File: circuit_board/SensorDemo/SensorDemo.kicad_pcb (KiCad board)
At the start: 2 copper layers, 65 x 57.5 mm, 43 parts, among them K1 PB, P1 CONN3X2, P2 CONN3X2, U1 TLV1117-33CDCYR, U2 dsPIC33EP32GP502, U3 LTC1658, U4 INA126, U5 REF1925, U6 REF1925, X1 CRYSTAL

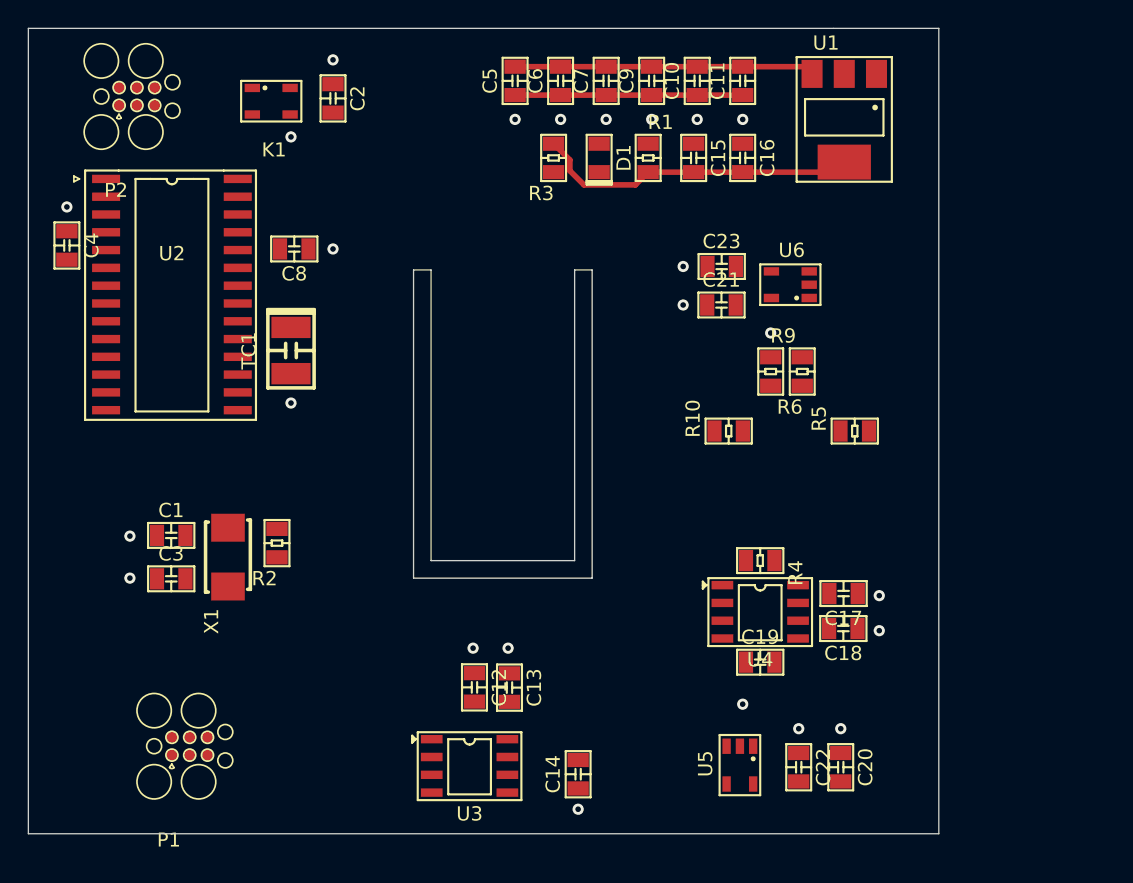
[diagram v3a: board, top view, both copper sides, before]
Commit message: symbol and pcb footprint updated
Added test points to replace the sensors.
TC2030 part modified.
the button needs modification.
TG connector:
https://www.tag-connect.com/product/tc2030-alt-nl-no-legs-cable-for-use-with-altera-usb-blaster
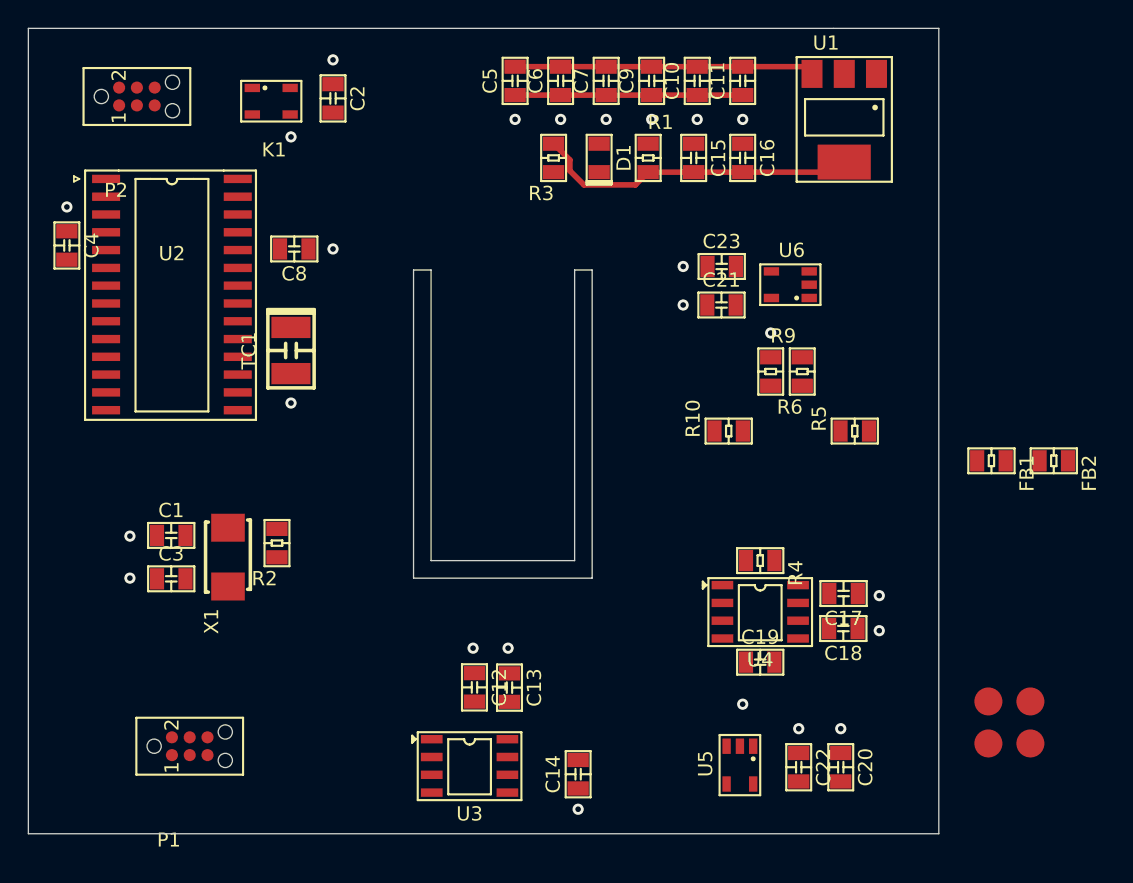
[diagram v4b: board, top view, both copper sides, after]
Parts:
- added FB1: 12.3071 nano ohm, SensorDemo_pcb:R0805, F.Cu at (186.3, 98.4)
- added FB2: 12.3071 nano ohm, SensorDemo_pcb:R0805, F.Cu at (190.7, 98.4)
- added TP1: TP, SensorDemo_pcb:TP_SMD_2MM, F.Cu at (186.0, 115.6)
- added TP2: TP, SensorDemo_pcb:TP_SMD_2MM, F.Cu at (186.0, 118.6)
- added TP3: TP, SensorDemo_pcb:TP_SMD_2MM, F.Cu at (189.0, 115.6)
- added TP4: TP, SensorDemo_pcb:TP_SMD_2MM, F.Cu at (189.0, 118.6)
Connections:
- K1 pad 1: Net-(K1-Pad1) -> (no net)
- K1 pad 3: Net-(K1-Pad3) -> (no net)
- P1 pad 1: (no net) -> /~MCLR
- P1 pad 2: (no net) -> /VDD
- P1 pad 4: (no net) -> /PGD
- P1 pad 5: (no net) -> /PGC
- P2 pad 1: (no net) -> /~MCLR
- P2 pad 2: (no net) -> /VDD
- P2 pad 3: (no net) -> GND
- P2 pad 4: (no net) -> /ucTX
- P2 pad 6: (no net) -> /ucRX
- U2 pad 10: Net-(U2-Pad10) -> (no net)
- U2 pad 11: Net-(U2-Pad11) -> (no net)
- U2 pad 12: Net-(U2-Pad12) -> (no net)
- U2 pad 14: Net-(U2-Pad14) -> (no net)
- U2 pad 18: Net-(U2-Pad18) -> (no net)
- U2 pad 23: Net-(U2-Pad23) -> (no net)
- U2 pad 24: Net-(U2-Pad24) -> (no net)
- U2 pad 25: Net-(U2-Pad25) -> (no net)
- U2 pad 26: Net-(U2-Pad26) -> (no net)
- U2 pad 3: Net-(U2-Pad3) -> (no net)
- U2 pad 9: Net-(U2-Pad9) -> (no net)
- U3 pad 4: Net-(U3-Pad4) -> (no net)
- U6 pad 1: Net-(U6-Pad1) -> (no net)
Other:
- copper layers 2 -> 4
- net class Default: clearance 0.2 -> 0.1524; trace_width 0.25 -> 0.1524; via_dia 0.8 -> 0.4; via_drill 0.4 -> 0.3
- rule trace_clearance: 0.2 -> 0.1524
- rule trace_min: 0.2 -> 0.1524
- rule via_min_size: 0.4 -> 0.3

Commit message: updated schematic
-fixed footprints
-spread parts
-connected some traces
- found FB (1kOhm, 1A)
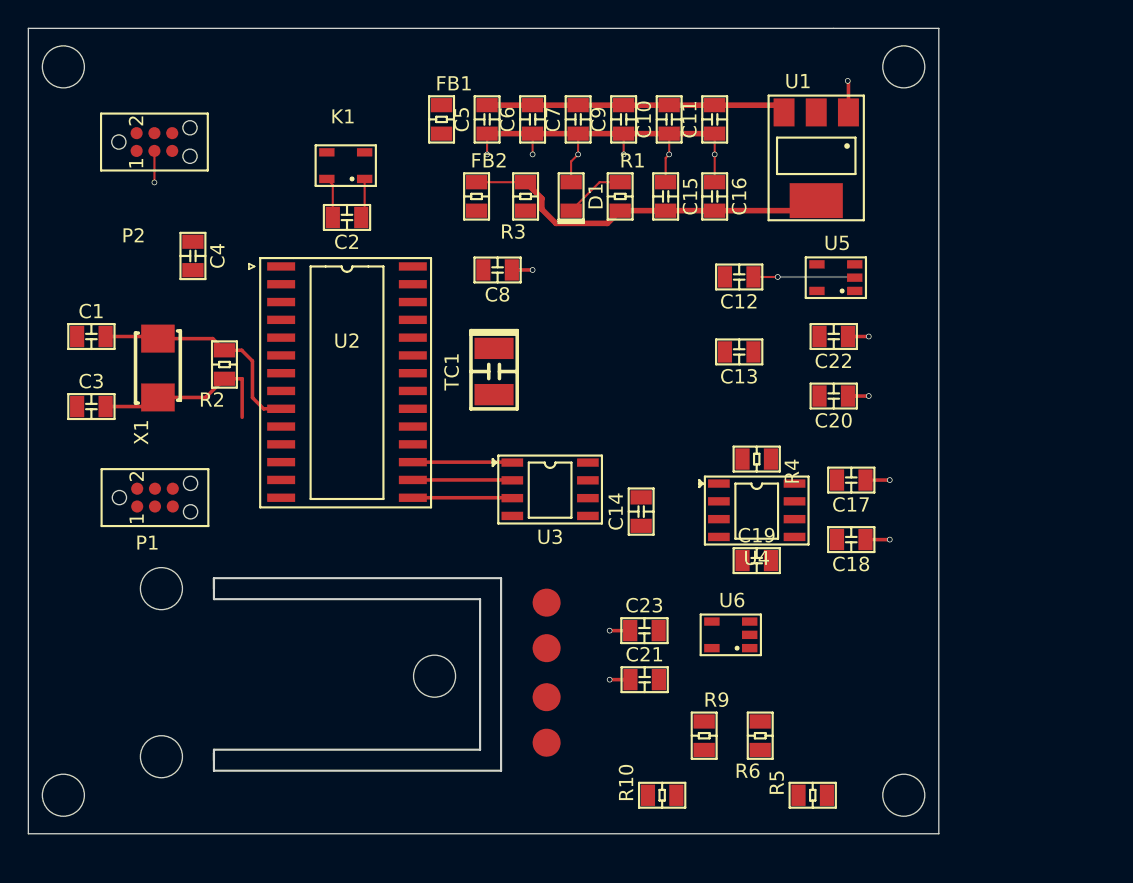
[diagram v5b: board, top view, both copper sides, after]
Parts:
- added MH1: MH, SensorDemo_pcb:MH_3MM, F.Cu at (120.0, 122.2)
- added MH2: MH, SensorDemo_pcb:MH_3MM, F.Cu at (127.0, 107.5)
- added MH3: MH, SensorDemo_pcb:MH_3MM, F.Cu at (180.0, 122.2)
- added MH4: MH, SensorDemo_pcb:MH_3MM, F.Cu at (127.0, 119.5)
- added MH5: MH, SensorDemo_pcb:MH_3MM, F.Cu at (120.0, 70.2)
- added MH6: MH, SensorDemo_pcb:MH_3MM, F.Cu at (146.5, 113.8)
- added MH7: MH, SensorDemo_pcb:MH_3MM, F.Cu at (180.0, 70.2)
- moved FB1 46.2 mm to (147.0, 74.0), turned to 90 degrees
- moved FB2 45.3 mm to (149.5, 79.5), turned to 90 degrees
- moved C12 34.9 mm to (168.2, 85.2), turned to 0 degrees
- moved TP3 34.7 mm to (154.5, 111.8)
- moved TP4 34.5 mm to (154.5, 118.5)
- moved U5 33.3 mm to (176.5, 86.2), turned to 180 degrees
- moved TP1 32.3 mm to (154.5, 108.5)
- moved TP2 31.7 mm to (154.5, 115.2)
- moved C22 30.9 mm to (175.0, 89.5), turned to 0 degrees
- moved C13 29.0 mm to (168.2, 90.6), turned to 0 degrees
- moved C21 27.3 mm to (161.5, 114.0)
- moved C23 26.6 mm to (161.5, 110.5)
- moved C20 26.5 mm to (175.0, 93.8), turned to 0 degrees
- moved R10 26.4 mm to (162.8, 122.2)
- moved R9 26.4 mm to (165.8, 118.0)
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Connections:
- C1 pad 1: Net-(C1-Pad1) -> /OSC1
- R2 pad 1: Net-(C1-Pad1) -> /OSC1
- U2 pad 10: (no net) -> /OSC1
- U2 pad 9: (no net) -> /OSC1
- X1 pad 1: Net-(C1-Pad1) -> /OSC1
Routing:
- net GND: track 16.2 -> 56.9 mm, vias 0 -> 16
- net /OSC1: track 0.00 -> 16.2 mm
- net Net-(C3-Pad1): track 0.00 -> 13.3 mm
- net Net-(U2-Pad17): track 0.00 -> 7.11 mm
- net Net-(U2-Pad16): track 0.00 -> 7.11 mm
- net Net-(U2-Pad15): track 0.00 -> 7.11 mm
- net Net-(D1-Pad1): track 0.00 -> 4.34 mm
- net +3V3: track 23.3 -> 26.8 mm
- net Net-(C2-Pad1): track 0.00 -> 2.93 mm
- net (no net): vias 24 -> 0
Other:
- outline, holes or cut-outs redrawn

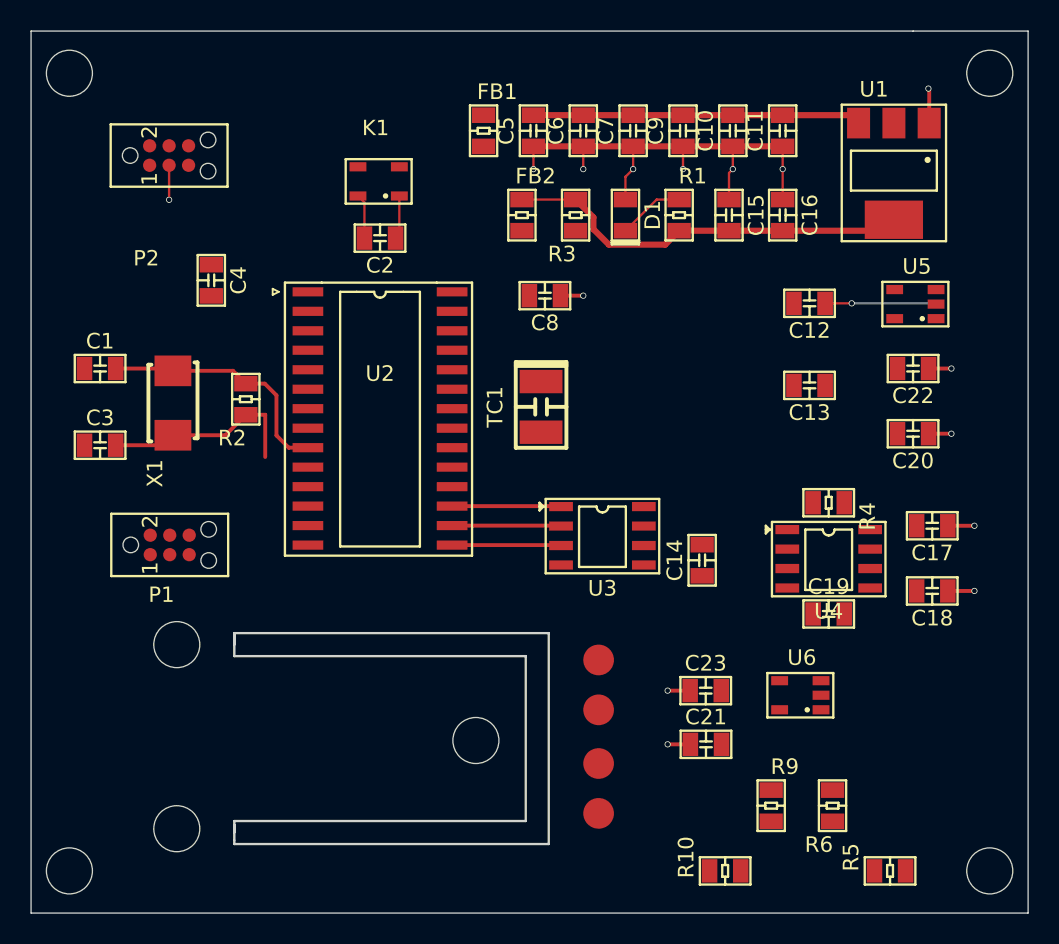
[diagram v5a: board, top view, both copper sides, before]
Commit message: update pcb
-connected traces
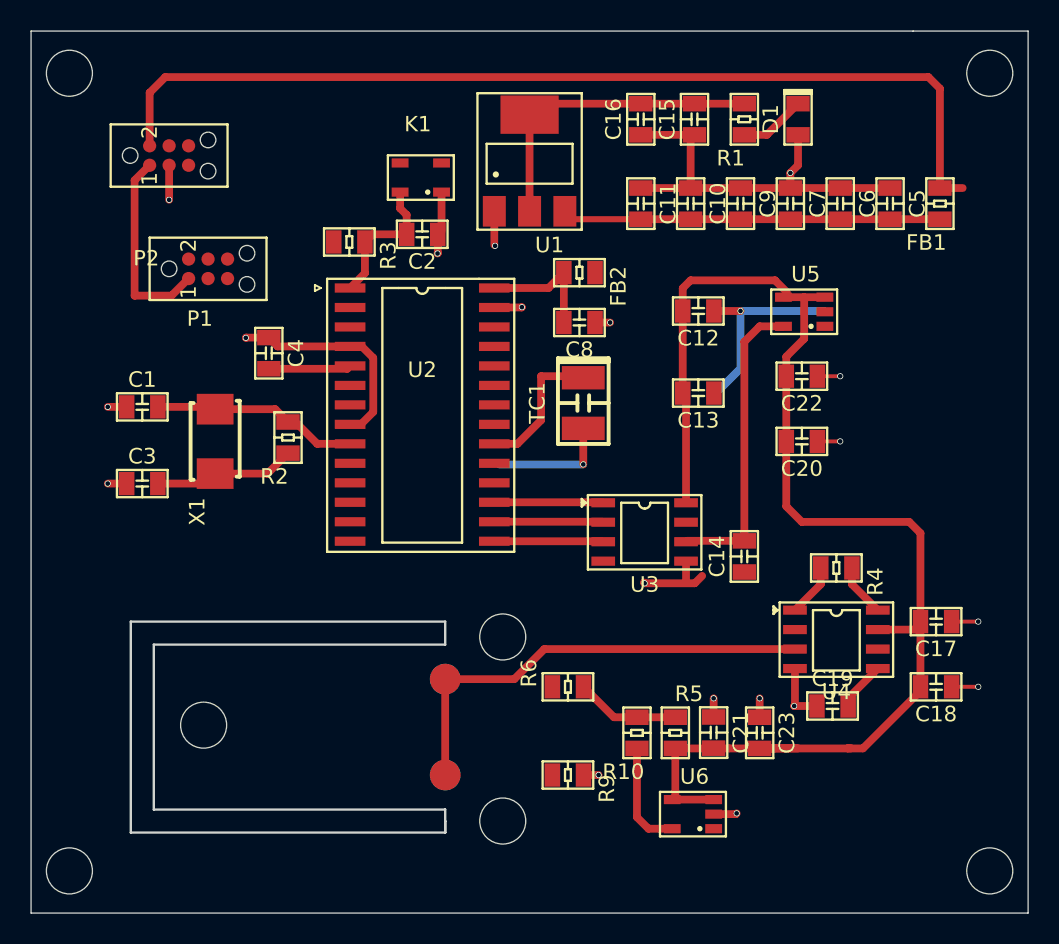
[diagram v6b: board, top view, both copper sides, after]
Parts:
- TP1, TP4: moved to B.Cu
- moved FB1 30.1 mm to (176.8, 78.8), turned to 270 degrees
- moved MH4 24.7 mm to (148.2, 107.0), turned to 180 degrees
- moved U1 24.4 mm to (150.0, 79.2), turned to 0 degrees
- moved MH2 24.2 mm to (148.2, 119.0), turned to 180 degrees
- moved C5 23.7 mm to (173.5, 78.8), turned to 90 degrees
- moved R6 18.9 mm to (152.5, 110.2), turned to 180 degrees
- moved P1 18.2 mm to (126.5, 83.0)
- moved MH6 17.8 mm to (128.8, 112.8), turned to 180 degrees
- moved C6 17.4 mm to (170.2, 78.8), turned to 90 degrees
- moved R5 16.6 mm to (159.5, 113.2), turned to 90 degrees
- moved R3 14.9 mm to (138.2, 81.2), turned to 0 degrees
- moved R9 13.4 mm to (152.5, 116.0), turned to 0 degrees
- moved D1 12.9 mm to (167.5, 73.2), turned to 270 degrees
- moved C7 11.3 mm to (167.0, 78.8), turned to 90 degrees
- moved C16 11.2 mm to (157.2, 73.2), turned to 270 degrees
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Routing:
- net +3V3: track 26.8 -> 109.3 mm
- net /VDD: track 0.00 -> 63.7 mm
- net GND: track 56.9 -> 96.6 mm, vias 16 -> 21
- net /Vsen: track 0.00 -> 29.9 mm
- net /Vref: track 0.00 -> 25.1 mm
- net /~MCLR: track 0.00 -> 12.9 mm
- net Net-(TC1-Pad1): track 0.00 -> 9.35 mm
- net Net-(C8-Pad1): track 0.00 -> 8.20 mm
- net Net-(R10-Pad2): track 0.00 -> 7.09 mm
- net Net-(R10-Pad1): track 0.00 -> 6.81 mm
- net Net-(C2-Pad1): track 2.93 -> 9.25 mm
- net Net-(C3-Pad1): track 13.3 -> 9.31 mm
- net Net-(R4-Pad2): track 0.00 -> 3.45 mm
- net Net-(R4-Pad1): track 0.00 -> 3.45 mm
- net Net-(C10-Pad1): track 21.4 -> 24.7 mm
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- added copper zone on GND, net GND
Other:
- outline, holes or cut-outs redrawn

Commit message: PCB edited
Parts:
- added C24: 1uF, SensorDemo_pcb:C0805, F.Cu at (129.8, 101.8)
- added C25: .1uF, SensorDemo_pcb:C0805, F.Cu at (133.8, 101.8)
- C1, C3: value C -> 22pF
- R10, R5: value 0 -> 0R
- R2: value R -> 1M
- TP1: moved to F.Cu
- TP3: moved to B.Cu
- X1: value CRYSTAL -> 8MHz
- moved P2 56.4 mm to (178.2, 91.0), turned to 90 degrees
- moved C18 30.5 mm to (170.0, 80.5)
- moved C17 22.7 mm to (170.0, 84.2)
- moved C16 18.0 mm to (139.5, 76.5), turned to 90 degrees
- moved C15 17.6 mm to (143.5, 76.5), turned to 90 degrees
- moved U5 16.2 mm to (153.0, 86.8), turned to 90 degrees
- moved U4 14.6 mm to (168.0, 90.8), turned to 90 degrees
- moved C2 13.6 mm to (129.5, 79.2), turned to 90 degrees
- moved R4 12.6 mm to (164.2, 91.2), turned to 90 degrees
- moved C20 12.4 mm to (158.5, 86.0), turned to 90 degrees
- moved K1 11.4 mm to (133.0, 76.0)
- moved C12 11.1 mm to (162.8, 96.8), turned to 90 degrees
- moved FB2 10.5 mm to (143.0, 81.0), turned to 180 degrees
- moved C23 7.50 mm to (168.8, 119.8), turned to 270 degrees
- moved C8 7.11 mm to (148.8, 81.0)
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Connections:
- C3 pad 1: Net-(C3-Pad1) -> /OSC2
- FB1 pad 1: /VDD -> Net-(FB1-Pad1)
- P1 pad 1: /~MCLR -> (no net)
- P1 pad 2: /VDD -> (no net)
- P2 pad 1: /~MCLR -> GND
- P2 pad 2: /VDD -> /ucTX
- P2 pad 4: /ucTX -> /ucRX
- P2 pad 5: (no net) -> Net-(FB1-Pad1)
- P2 pad 6: /ucRX -> Net-(FB1-Pad1)
- R2 pad 2: Net-(C3-Pad1) -> /OSC2
- U2 pad 10: /OSC1 -> /OSC2
- X1 pad 2: Net-(C3-Pad1) -> /OSC2
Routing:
- net +3V3: track 109.3 -> 24.1 mm, vias 0 -> 6
- net GND: track 96.6 -> 27.4 mm, vias 21 -> 8
- net /VDD: track 63.7 -> 0.00 mm
- net /ucRX: track 0.00 -> 31.3 mm, vias 0 -> 2
- net /ucTX: track 0.00 -> 31.3 mm, vias 0 -> 2
- net /Vsen: track 29.9 -> 0.00 mm
- net /OSC2: track 0.00 -> 13.9 mm
- net /~MCLR: track 12.9 -> 0.00 mm
- net Net-(TC1-Pad1): track 9.35 -> 0.00 mm
- net Net-(C3-Pad1): track 9.31 -> 0.00 mm
- net Net-(C2-Pad1): track 9.25 -> 0.00 mm
- net Net-(C8-Pad1): track 8.20 -> 0.00 mm
- net Net-(U2-Pad17): track 7.11 -> 0.00 mm
- net Net-(U2-Pad16): track 7.11 -> 0.00 mm
- net Net-(U2-Pad15): track 7.11 -> 0.00 mm
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- added copper zone on PWR, net +3V3
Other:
- outline, holes or cut-outs redrawn
